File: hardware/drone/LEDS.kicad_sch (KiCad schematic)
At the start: 12 parts, among them Q103 IRLML6402TRPBF, Q104 IRLML6402TRPBF

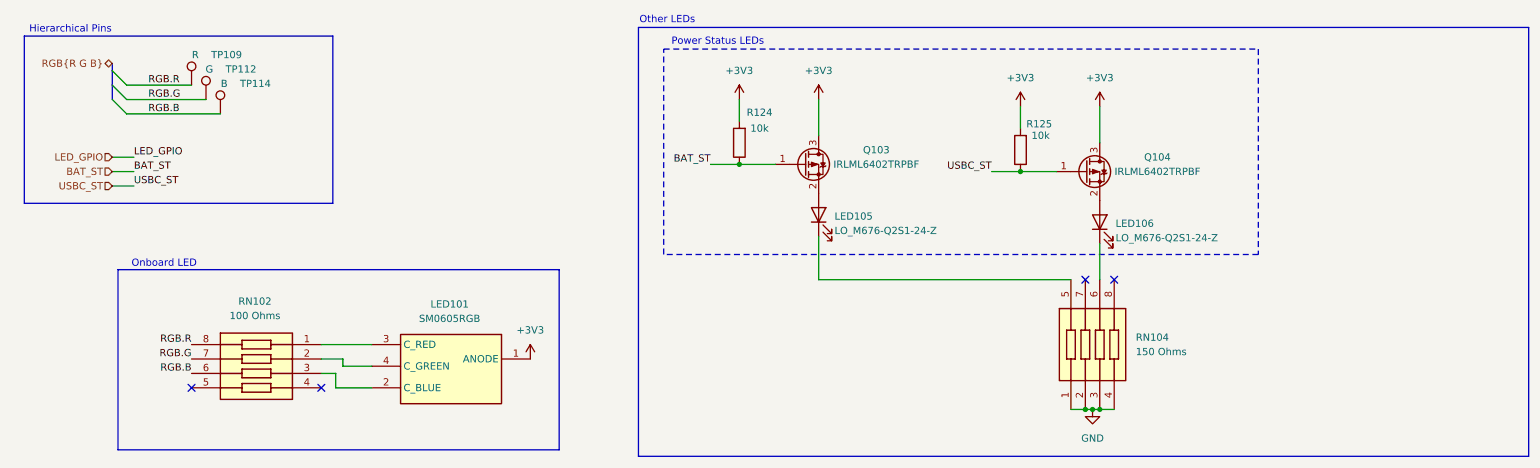
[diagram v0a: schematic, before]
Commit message: save before axing motor driver ic's
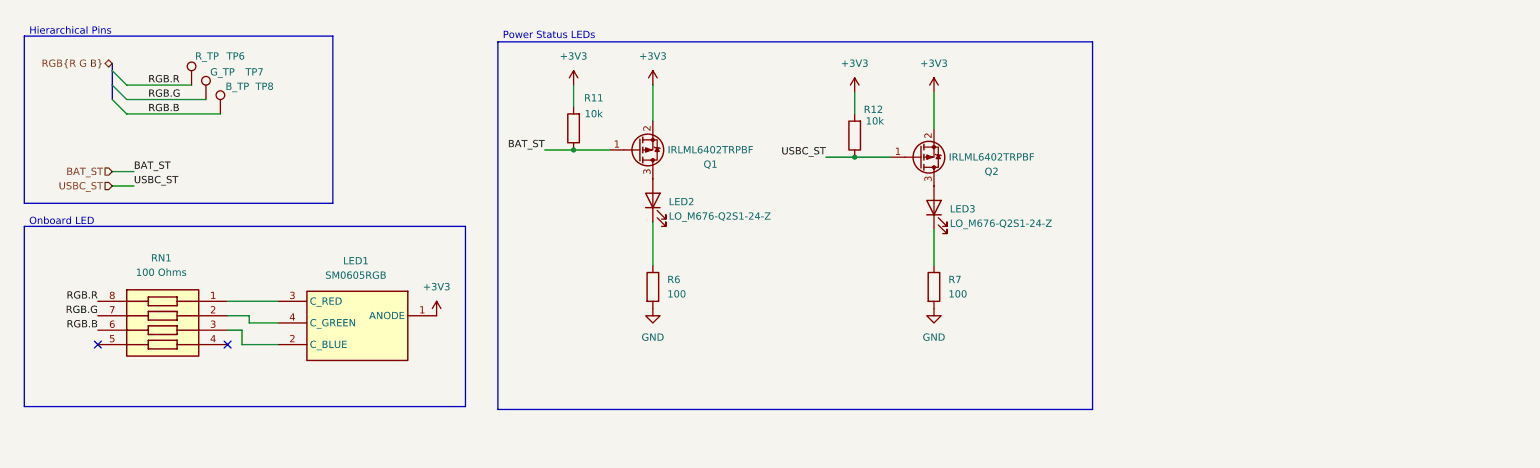
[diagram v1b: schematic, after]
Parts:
- removed RN104: 150 Ohms, SamacSys_Parts:EXBV8V151JV, symbol SamacSys_Parts:EXB-V8V151JV
- added R6, R7: 100, SamacSys_Parts:RESC1608X55N, symbol Device:R
- TP6: renamed from TP109; value R -> R_TP; footprint TestPoint:TestPoint_Pad_1.0x1.0mm -> SamacSys_Parts:TestPoint_Pad_1.0x1.0mm
- TP7: renamed from TP112; value G -> G_TP; footprint TestPoint:TestPoint_Pad_1.0x1.0mm -> SamacSys_Parts:TestPoint_Pad_1.0x1.0mm
- TP8: renamed from TP114; value B -> B_TP; footprint TestPoint:TestPoint_Pad_1.0x1.0mm -> SamacSys_Parts:TestPoint_Pad_1.0x1.0mm
- renumbered LED101 to LED1, LED105 to LED2, LED106 to LED3, Q103 to Q1, Q104 to Q2, R124 to R11, R125 to R12, RN102 to RN1
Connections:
- net +3V3: now also Q1.2 (S), Q2.2 (S); no longer Q1.3 (D), Q2.3 (D)
- net GND: now also R6.2, R7.2
- net at LED3.2 (A): now also Q2.3 (D); no longer Q2.2 (S)
- net at LED3.1 (K): now also R7.1
- net at LED2.2 (A): now also Q1.3 (D); no longer Q1.2 (S)
- net at LED2.1 (K): now also R6.1
- no-connect marks 4 -> 2
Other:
- note removed: "Other LEDs"
- moved on the sheet: LED1, LED2, LED3, Q1, Q2, R11, R12, RN1

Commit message: axed motor drivers. finished layout for drone but need to review overall system design after reading some stuff
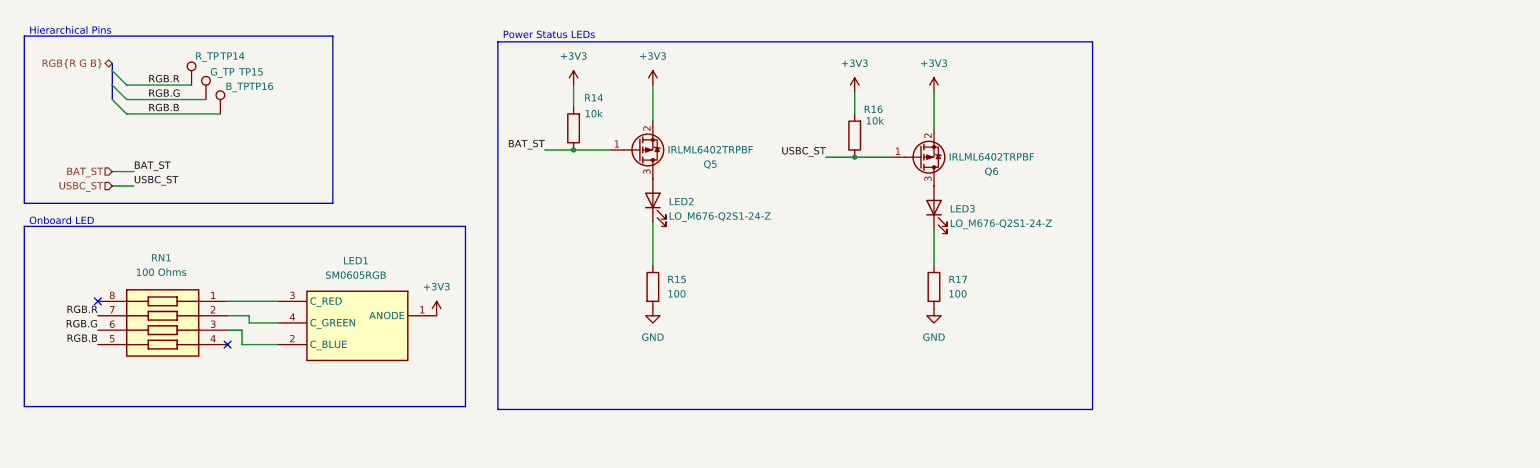
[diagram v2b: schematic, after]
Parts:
- renumbered Q1 to Q5, Q2 to Q6, R11 to R14, R6 to R15, R12 to R16, R7 to R17, TP6 to TP14, TP7 to TP15, TP8 to TP16
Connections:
- net RGB.B: now also RN1.5; no longer RN1.6
- net RGB.G: now also RN1.6; no longer RN1.7
- net RGB.R: now also RN1.7; no longer RN1.8
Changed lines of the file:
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@@
 	)
 	(no_connect
-		(at 29.21 73.66)
+		(at 29.21 66.04)
 	)
 	(no_connect
@@
 	)
 	(label "RGB.B"
-		(at 29.21 71.12 180)
+		(at 29.21 73.66 180)
 		(effects
 			(font
@@
 	)
 	(label "RGB.R"
-		(at 29.21 66.04 180)
+		(at 29.21 68.58 180)
 		(effects
 			(font
@@
 	)
 	(label "RGB.G"
-		(at 29.21 68.58 180)
+		(at 29.21 71.12 180)
 		(effects
 			(font
@@
 		(on_board yes)
 		(dnp no)
-		(property "Reference" "TP6"
+		(property "Reference" "TP14"
 			(at 55.118 22.86 0)
 			(effects
@@
 			(project "drone"
 				(path "/869bea87-c885-4ead-826b-3f34ceacafad/1db4bee0-4e23-41b0-8f30-8f71981fa175"
-					(reference "TP6")
+					(reference "TP14")
 					(unit 1)
 				)
@@
 		(on_board yes)
 		(dnp no)
-		(property "Reference" "R12"
+		(property "Reference" "R16"
 			(at 165.862 32.258 0)
 			(effects
@@
 			(project "controller"
 				(path "/869bea87-c885-4ead-826b-3f34ceacafad/1db4bee0-4e23-41b0-8f30-8f71981fa175"
-					(reference "R12")
+					(reference "R16")
 					(unit 1)
 				)
@@
 		(on_board yes)
 		(dnp no)
-		(property "Reference" "Q2"
+		(property "Reference" "Q6"
 			(at 186.69 43.18 0)
 			(effects
@@
 			(project "controller"
 				(path "/869bea87-c885-4ead-826b-3f34ceacafad/1db4bee0-4e23-41b0-8f30-8f71981fa175"
-					(reference "Q2")
+					(reference "Q6")
 					(unit 1)
 				)
@@
 		(dnp no)
 		(fields_autoplaced yes)
-		(property "Reference" "#PWR049"
+		(property "Reference" "#PWR068"
 			(at 176.53 73.66 0)
 			(effects
@@
 			(project ""
 				(path "/869bea87-c885-4ead-826b-3f34ceacafad/1db4bee0-4e23-41b0-8f30-8f71981fa175"
-					(reference "#PWR049")
+					(reference "#PWR068")
 					(unit 1)
 				)
@@
 		(dnp no)
 		(fields_autoplaced yes)
-		(property "Reference" "R7"
+		(property "Reference" "R17"
 			(at 179.07 62.2299 0)
 			(effects
@@
 			(project "drone"
 				(path "/869bea87-c885-4ead-826b-3f34ceacafad/1db4bee0-4e23-41b0-8f30-8f71981fa175"
-					(reference "R7")
+					(reference "R17")
 					(unit 1)
 				)
@@
 		(dnp no)
 		(fields_autoplaced yes)
-		(property "Reference" "#PWR045"
+		(property "Reference" "#PWR062"
 			(at 88.9 72.39 0)
 			(effects
@@
 			(project "drone"
 				(path "/869bea87-c885-4ead-826b-3f34ceacafad/1db4bee0-4e23-41b0-8f30-8f71981fa175"
-					(reference "#PWR045")
+					(reference "#PWR062")
 					(unit 1)
 				)
@@
 		(on_board yes)
 		(dnp no)
-		(property "Reference" "Q1"
+		(property "Reference" "Q5"
 			(at 137.16 41.91 0)
 			(effects
@@
 			(project "controller"
 				(path "/869bea87-c885-4ead-826b-3f34ceacafad/1db4bee0-4e23-41b0-8f30-8f71981fa175"
-					(reference "Q1")
+					(reference "Q5")
 					(unit 1)
 				)
@@
 		(dnp no)
 		(fields_autoplaced yes)
-		(property "Reference" "#PWR057"
+		(property "Reference" "#PWR065"
 			(at 127 73.66 0)
 			(effects
@@
 			(project "drone"
 				(path "/869bea87-c885-4ead-826b-3f34ceacafad/1db4bee0-4e23-41b0-8f30-8f71981fa175"
-					(reference "#PWR057")
+					(reference "#PWR065")
 					(unit 1)
 				)
@@
 		(on_board yes)
 		(dnp no)
-		(property "Reference" "R11"
+		(property "Reference" "R14"
 			(at 116.586 30.226 0)
 			(effects
@@
 			(project "controller"
 				(path "/869bea87-c885-4ead-826b-3f34ceacafad/1db4bee0-4e23-41b0-8f30-8f71981fa175"
-					(reference "R11")
+					(reference "R14")
 					(unit 1)
 				)
@@
 		(dnp no)
 		(fields_autoplaced yes)
-		(property "Reference" "#PWR046"
+		(property "Reference" "#PWR063"
 			(at 113.03 31.75 0)
 			(effects
@@
 			(project "controller"
 				(path "/869bea87-c885-4ead-826b-3f34ceacafad/1db4bee0-4e23-41b0-8f30-8f71981fa175"
-					(reference "#PWR046")
+					(reference "#PWR063")
 					(unit 1)
 				)
@@
 		(on_board yes)
 		(dnp no)
-		(property "Reference" "TP7"
+		(property "Reference" "TP15"
 			(at 58.42 25.654 0)
 			(effects
@@
 			(project "drone"
 				(path "/869bea87-c885-4ead-826b-3f34ceacafad/1db4bee0-4e23-41b0-8f30-8f71981fa175"
-					(reference "TP7")
+					(reference "TP15")
 					(unit 1)
 				)
@@
 		(dnp no)
 		(fields_autoplaced yes)
-		(property "Reference" "#PWR047"
+		(property "Reference" "#PWR064"
 			(at 127 31.75 0)
 			(effects
@@
 			(project "controller"
 				(path "/869bea87-c885-4ead-826b-3f34ceacafad/1db4bee0-4e23-41b0-8f30-8f71981fa175"
-					(reference "#PWR047")
+					(reference "#PWR064")
 					(unit 1)
 				)
@@
 		(dnp no)
 		(fields_autoplaced yes)
-		(property "Reference" "R6"
+		(property "Reference" "R15"
 			(at 129.54 62.2299 0)
 			(effects
@@
 			(project "drone"
 				(path "/869bea87-c885-4ead-826b-3f34ceacafad/1db4bee0-4e23-41b0-8f30-8f71981fa175"
-					(reference "R6")
+					(reference "R15")
 					(unit 1)
 				)
@@
 		(dnp no)
 		(fields_autoplaced yes)
-		(property "Reference" "#PWR050"
+		(property "Reference" "#PWR067"
 			(at 176.53 33.02 0)
 			(effects
@@
 			(project "controller"
 				(path "/869bea87-c885-4ead-826b-3f34ceacafad/1db4bee0-4e23-41b0-8f30-8f71981fa175"
-					(reference "#PWR050")
+					(reference "#PWR067")
 					(unit 1)
 				)
@@
 		(dnp no)
 		(fields_autoplaced yes)
-		(property "Reference" "#PWR048"
+		(property "Reference" "#PWR066"
 			(at 162.56 33.02 0)
 			(effects
@@
 			(project "controller"
 				(path "/869bea87-c885-4ead-826b-3f34ceacafad/1db4bee0-4e23-41b0-8f30-8f71981fa175"
-					(reference "#PWR048")
+					(reference "#PWR066")
 					(unit 1)
 				)
@@
 		(on_board yes)
 		(dnp no)
-		(property "Reference" "TP8"
+		(property "Reference" "TP16"
 			(at 60.198 28.194 0)
 			(effects
@@
 			(project "drone"
 				(path "/869bea87-c885-4ead-826b-3f34ceacafad/1db4bee0-4e23-41b0-8f30-8f71981fa175"
-					(reference "TP8")
+					(reference "TP16")
 					(unit 1)
 				)
